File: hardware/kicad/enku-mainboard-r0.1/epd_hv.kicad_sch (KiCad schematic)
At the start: 2 parts

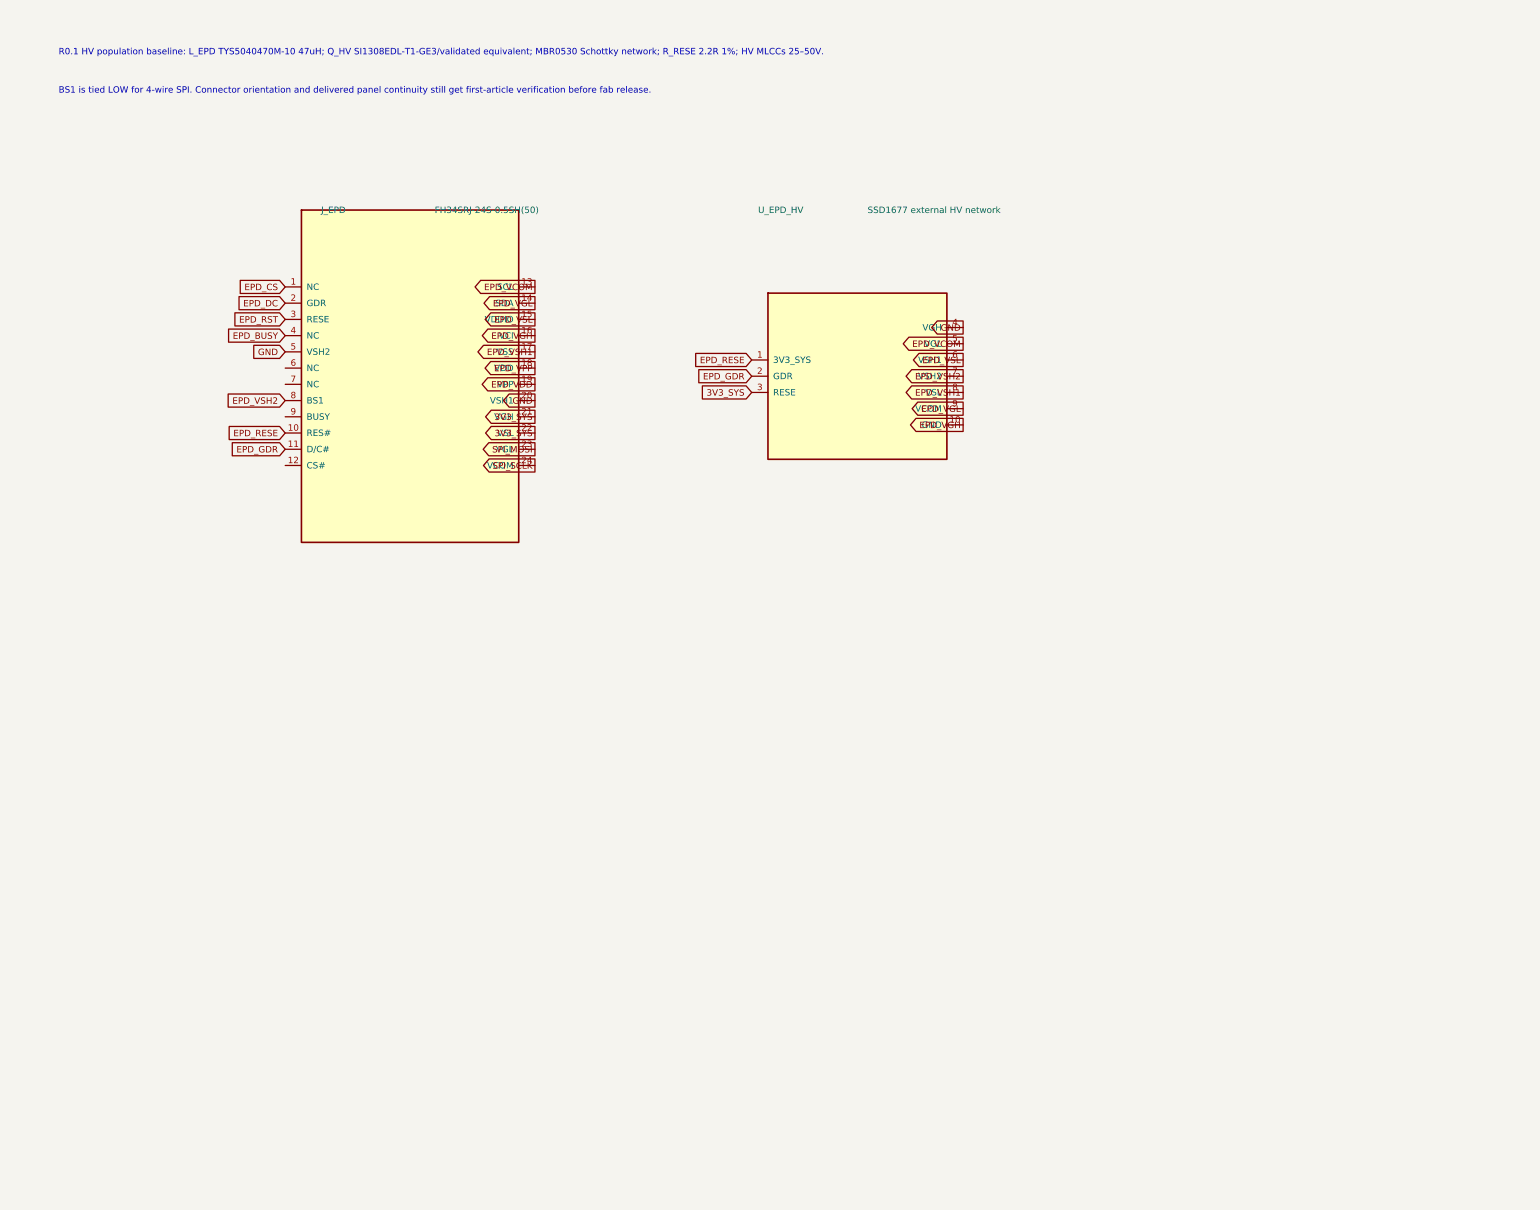
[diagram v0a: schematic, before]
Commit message: Expand SSD1677 EPD HV reference circuit to discretes
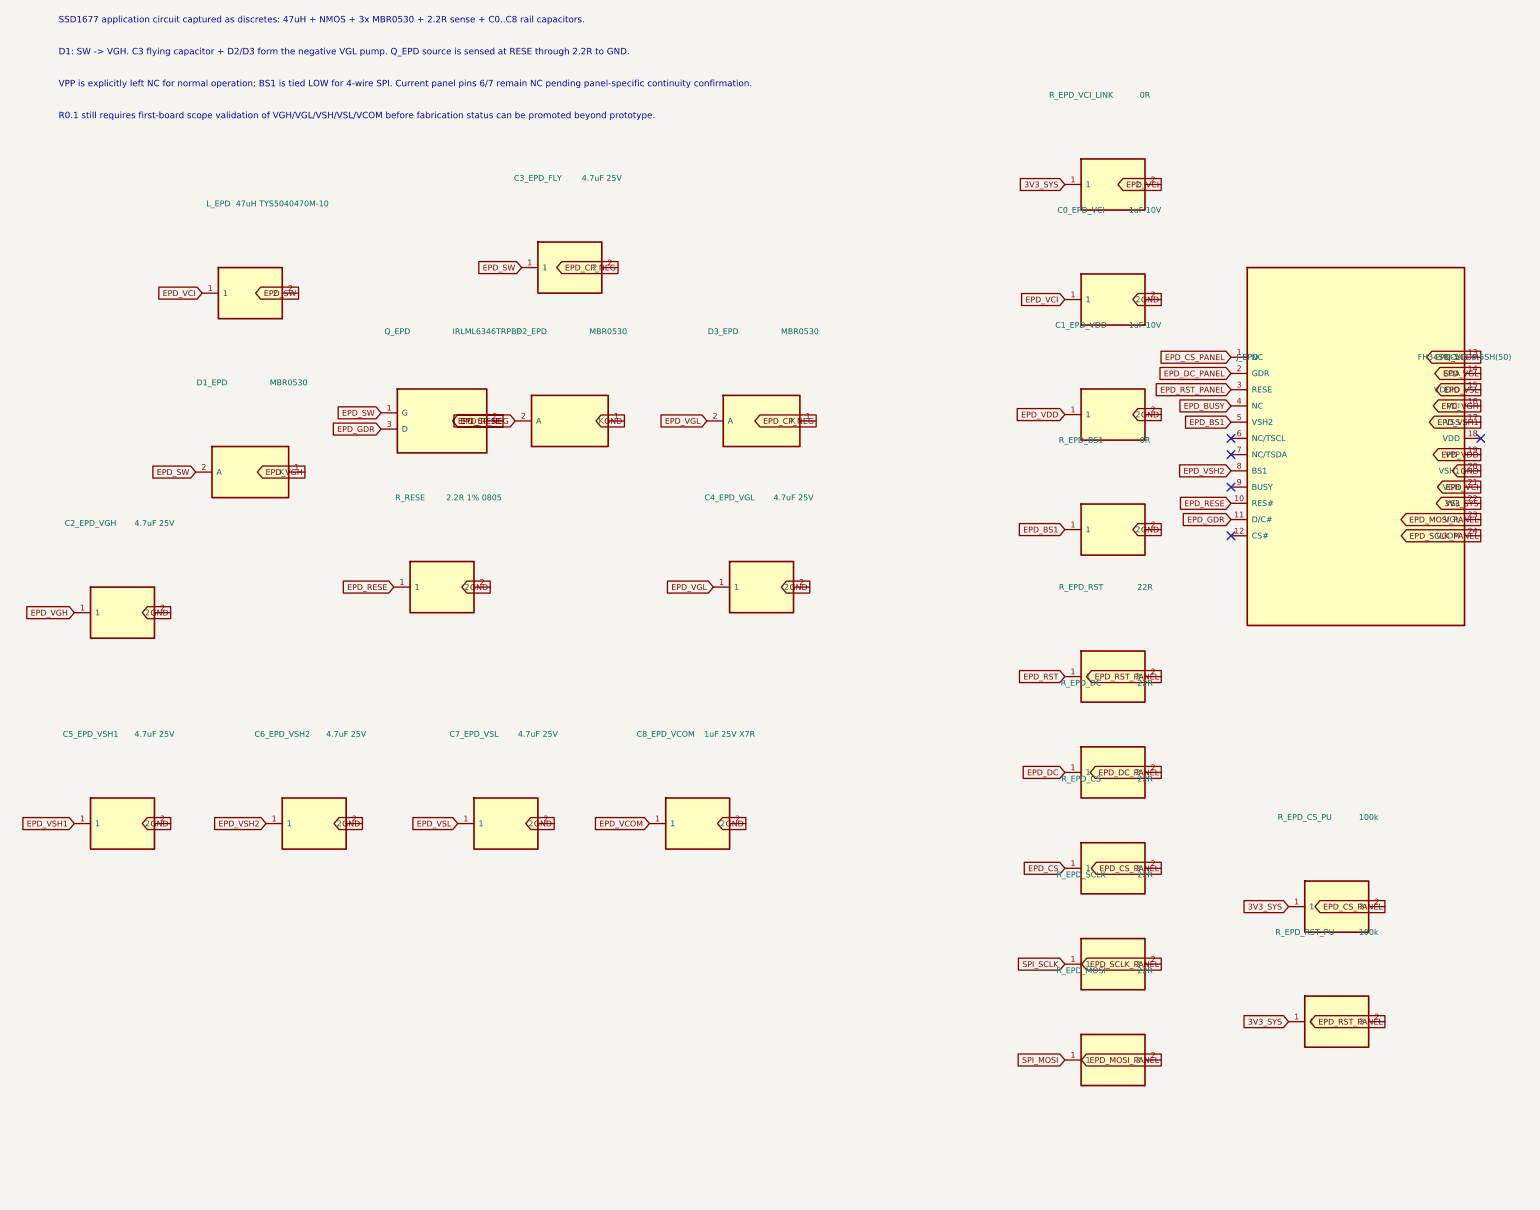
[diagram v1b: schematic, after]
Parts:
- removed J_EPD: FH34SRJ-24S-0.5SH(50), ENKU:R0.1_FH34SRJ_24_DUAL_CONTACT_PLACEHOLDER, symbol ENKU:EPD_FPC_24
- removed U_EPD_HV: SSD1677 external HV network, symbol ENKU:EPD_HV_NETWORK
- added C0_EPD_VCI, C1_EPD_VDD: 1uF 10V, Capacitor_SMD:C_0603_1608Metric, symbol ENKU:C
- added C2_EPD_VGH, C3_EPD_FLY, C4_EPD_VGL, C5_EPD_VSH1, C6_EPD_VSH2, C7_EPD_VSL: 4.7uF 25V, Capacitor_SMD:C_0805_2012Metric, symbol ENKU:C
- added C8_EPD_VCOM: 1uF 25V X7R, Capacitor_SMD:C_0805_2012Metric, symbol ENKU:C
- added D1_EPD, D2_EPD, D3_EPD: MBR0530, Diode_SMD:D_SOD-123, symbol ENKU:D_SCHOTTKY
- added J_EPD: FH34SRJ-24S-0.5SH(50), ENKU:R0.1_FH34SRJ_24_DUAL_CONTACT_PLACEHOLDER, symbol ENKU:EPD_FPC24
- added L_EPD: 47uH TYS5040470M-10, ENKU:TYS5040470M-10, symbol ENKU:L
- added Q_EPD: IRLML6346TRPBF, Package_TO_SOT_SMD:SOT-23, symbol ENKU:NMOS
- added R_EPD_BS1, R_EPD_VCI_LINK: 0R, Resistor_SMD:R_0603_1608Metric, symbol ENKU:R
- added R_EPD_CS, R_EPD_DC, R_EPD_MOSI, R_EPD_RST, R_EPD_SCLK: 22R, Resistor_SMD:R_0603_1608Metric, symbol ENKU:R
- added R_EPD_CS_PU, R_EPD_RST_PU: 100k, Resistor_SMD:R_0603_1608Metric, symbol ENKU:R
- added R_RESE: 2.2R 1% 0805, Resistor_SMD:R_0805_2012Metric, symbol ENKU:R
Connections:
- net 3V3_SYS: now also J_EPD.22 (VSL), R_EPD_CS_PU.1, R_EPD_RST_PU.1, R_EPD_VCI_LINK.1
- net EPD_BUSY: now also J_EPD.4 (NC)
- net EPD_CS: now also R_EPD_CS.1
- net EPD_DC: now also R_EPD_DC.1
- net EPD_GDR: now also J_EPD.11 (D/C#), Q_EPD.3 (D)
- net EPD_RESE: now also J_EPD.10 (RES#), Q_EPD.2 (S), R_RESE.1
- net EPD_RST: now also R_EPD_RST.1
- net EPD_VCOM: now also C8_EPD_VCOM.1, J_EPD.13 (SCL)
- net EPD_VDD: now also C1_EPD_VDD.1, J_EPD.19 (VPP)
- net EPD_VGH: now also C2_EPD_VGH.1, D1_EPD.1 (K), J_EPD.16 (VCI)
- net EPD_VGL: now also C4_EPD_VGL.1, D3_EPD.2 (A), J_EPD.14 (SDA)
- net EPD_VSH1: now also C5_EPD_VSH1.1, J_EPD.17 (VSS)
- net EPD_VSH2: now also C6_EPD_VSH2.1, J_EPD.8 (BS1)
- net EPD_VSL: now also C7_EPD_VSL.1, J_EPD.15 (VDDIO)
- net GND: now also C0_EPD_VCI.2, C1_EPD_VDD.2, C2_EPD_VGH.2, C4_EPD_VGL.2, C5_EPD_VSH1.2, C6_EPD_VSH2.2, C7_EPD_VSL.2, C8_EPD_VCOM.2, D2_EPD.1 (K), J_EPD.20 (VSH1), R_EPD_BS1.2, R_RESE.2
- net SPI_MOSI: now also R_EPD_MOSI.1
- net SPI_SCLK: now also R_EPD_SCLK.1
- new net EPD_BS1: J_EPD.5 (VSH2), R_EPD_BS1.1
- new net EPD_CP_NEG: C3_EPD_FLY.2, D2_EPD.2 (A), D3_EPD.1 (K)
- new net EPD_CS_PANEL: J_EPD.1 (NC), R_EPD_CS.2, R_EPD_CS_PU.2
- new net EPD_DC_PANEL: J_EPD.2 (GDR), R_EPD_DC.2
- new net EPD_MOSI_PANEL: J_EPD.23 (VGL), R_EPD_MOSI.2
- new net EPD_RST_PANEL: J_EPD.3 (RESE), R_EPD_RST.2, R_EPD_RST_PU.2
- new net EPD_SCLK_PANEL: J_EPD.24 (VCOM), R_EPD_SCLK.2
- new net EPD_SW: C3_EPD_FLY.1, D1_EPD.2 (A), L_EPD.2, Q_EPD.1 (G)
- new net EPD_VCI: C0_EPD_VCI.1, J_EPD.21 (VGH), L_EPD.1, R_EPD_VCI_LINK.2
- no-connect marks 0 -> 5
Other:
- note added: "D1: SW -> VGH. C3 flying capacitor + D2/D3 form the negative VGL pump. Q_EPD source is sensed at RESE through 2.2R to GND."
- note added: "R0.1 still requires first-board scope validation of VGH/VGL/VSH/VSL/VCOM before fabrication status can be promoted beyond prototype."
- note added: "SSD1677 application circuit captured as discretes: 47uH + NMOS + 3x MBR0530 + 2.2R sense + C0..C8 rail capacitors."
- note added: "VPP is explicitly left NC for normal operation; BS1 is tied LOW for 4-wire SPI. Current panel pins 6/7 remain NC pending panel-specific continuity confirmation."
- note removed: "BS1 is tied LOW for 4-wire SPI. Connector orientation and delivered panel continuity still get first-article verification before fab release."
- note removed: "R0.1 HV population baseline: L_EPD TYS5040470M-10 47uH; Q_HV SI1308EDL-T1-GE3/validated equivalent; MBR0530 Schottky network; R_RESE 2.2R 1%; HV MLCCs 25–50V."
- title: ENKU R0.1 — EPD + HV -> ENKU R0.1 — SSD1677 EPD + HV

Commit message: Align EPD boost baseline with current 3.97-inch application circuit
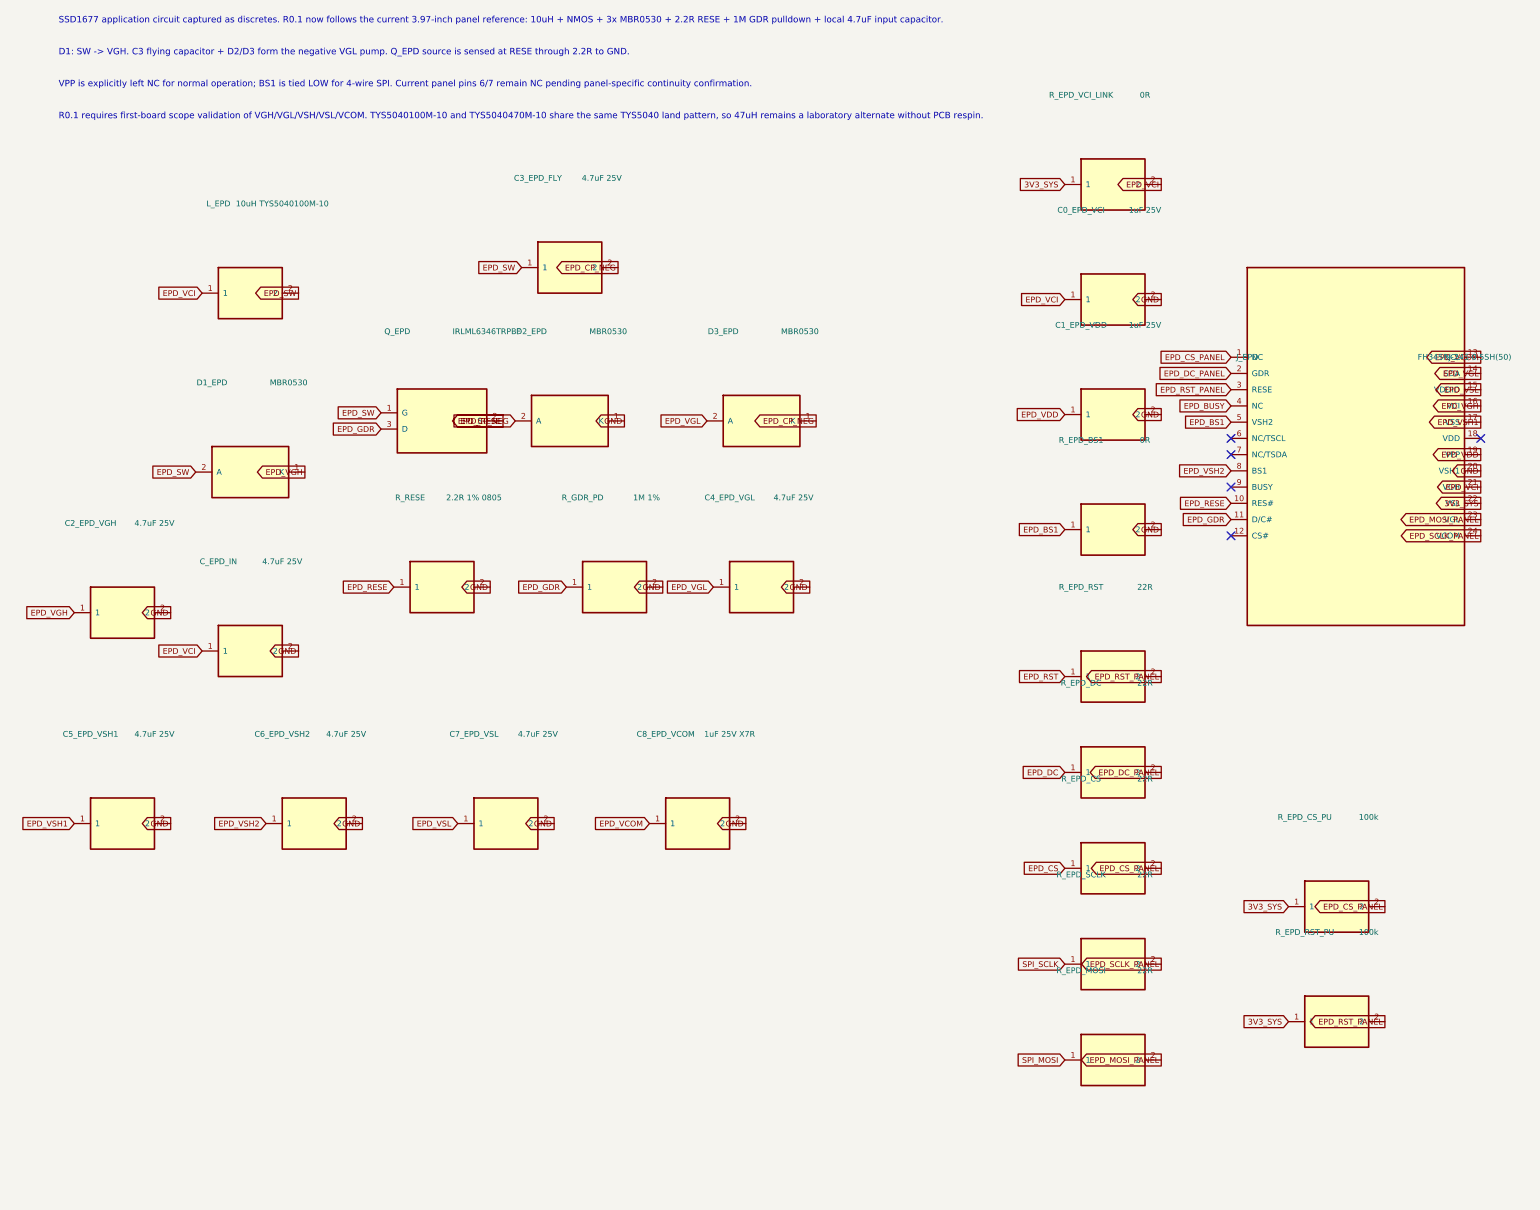
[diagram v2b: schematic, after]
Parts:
- added C_EPD_IN: 4.7uF 25V, Capacitor_SMD:C_0805_2012Metric, symbol ENKU:C
- added R_GDR_PD: 1M 1%, Resistor_SMD:R_0603_1608Metric, symbol ENKU:R
- C0_EPD_VCI, C1_EPD_VDD: value 1uF 10V -> 1uF 25V
- L_EPD: value 47uH TYS5040470M-10 -> 10uH TYS5040100M-10; footprint ENKU:TYS5040470M-10 -> ENKU:TYS5040_5x5
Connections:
- net EPD_GDR: now also R_GDR_PD.1
- net EPD_VCI: now also C_EPD_IN.1
- net GND: now also C_EPD_IN.2, R_GDR_PD.2
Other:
- note added: "R0.1 requires first-board scope validation of VGH/VGL/VSH/VSL/VCOM. TYS5040100M-10 and TYS5040470M-10 share the same TYS5040 land pattern, so 47uH remains a laboratory alternate without PCB respin."
- note added: "SSD1677 application circuit captured as discretes. R0.1 now follows the current 3.97-inch panel reference: 10uH + NMOS + 3x MBR0530 + 2.2R RESE + 1M GDR pulldown + local 4.7uF input capacitor."
- note removed: "R0.1 still requires first-board scope validation of VGH/VGL/VSH/VSL/VCOM before fabrication status can be promoted beyond prototype."
- note removed: "SSD1677 application circuit captured as discretes: 47uH + NMOS + 3x MBR0530 + 2.2R sense + C0..C8 rail capacitors."
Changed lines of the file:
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@@
 	(symbol (lib_id "ENKU:C") (at 190 63 0) (unit 1) (exclude_from_sim no) (in_bom yes) (on_board yes) (dnp no)
 		(property "Reference" "C0_EPD_VCI" (at 185 49 0) (effects (font (size 0.9 0.9))))
-		(property "Value" "1uF 10V" (at 195 49 0) (effects (font (size 0.9 0.9))))
+		(property "Value" "1uF 25V" (at 195 49 0) (effects (font (size 0.9 0.9))))
 		(property "Footprint" "Capacitor_SMD:C_0603_1608Metric" (at 190 63 0) (effects (font (size 0.9 0.9)) (hide yes)))
 		(property "Datasheet" "~" (at 190 63 0) (effects (font (size 0.9 0.9)) (hide yes)))
-		(property "Description" "1uF 10V" (at 190 63 0) (effects (font (size 0.9 0.9)) (hide yes)))
+		(property "Description" "1uF 25V" (at 190 63 0) (effects (font (size 0.9 0.9)) (hide yes)))
 		(pin "1")
 		(pin "2")
@@
 	(symbol (lib_id "ENKU:C") (at 190 81 0) (unit 1) (exclude_from_sim no) (in_bom yes) (on_board yes) (dnp no)
 		(property "Reference" "C1_EPD_VDD" (at 185 67 0) (effects (font (size 0.9 0.9))))
-		(property "Value" "1uF 10V" (at 195 67 0) (effects (font (size 0.9 0.9))))
+		(property "Value" "1uF 25V" (at 195 67 0) (effects (font (size 0.9 0.9))))
 		(property "Footprint" "Capacitor_SMD:C_0603_1608Metric" (at 190 81 0) (effects (font (size 0.9 0.9)) (hide yes)))
 		(property "Datasheet" "~" (at 190 81 0) (effects (font (size 0.9 0.9)) (hide yes)))
-		(property "Description" "1uF 10V" (at 190 81 0) (effects (font (size 0.9 0.9)) (hide yes)))
+		(property "Description" "1uF 25V" (at 190 81 0) (effects (font (size 0.9 0.9)) (hide yes)))
 		(pin "1")
 		(pin "2")
@@
 	(symbol (lib_id "ENKU:L") (at 55 62 0) (unit 1) (exclude_from_sim no) (in_bom yes) (on_board yes) (dnp no)
 		(property "Reference" "L_EPD" (at 50 48 0) (effects (font (size 0.9 0.9))))
-		(property "Value" "47uH TYS5040470M-10" (at 60 48 0) (effects (font (size 0.9 0.9))))
-		(property "Footprint" "ENKU:TYS5040470M-10" (at 55 62 0) (effects (font (size 0.9 0.9)) (hide yes)))
+		(property "Value" "10uH TYS5040100M-10" (at 60 48 0) (effects (font (size 0.9 0.9))))
+		(property "Footprint" "ENKU:TYS5040_5x5" (at 55 62 0) (effects (font (size 0.9 0.9)) (hide yes)))
 		(property "Datasheet" "~" (at 55 62 0) (effects (font (size 0.9 0.9)) (hide yes)))
-		(property "Description" "47uH TYS5040470M-10" (at 55 62 0) (effects (font (size 0.9 0.9)) (hide yes)))
+		(property "Description" "10uH TYS5040100M-10" (at 55 62 0) (effects (font (size 0.9 0.9)) (hide yes)))
 		(pin "1")
 		(pin "2")
@@
 	(global_label "EPD_VCOM" (shape input) (at 117.46 145 0) (effects (font (size 0.9 0.9)) (justify right bottom)))
 	(global_label "GND" (shape output) (at 132.54 145 180) (effects (font (size 0.9 0.9)) (justify right bottom)))
-	(text "SSD1677 application circuit captured as discretes: 47uH + NMOS + 3x MBR0530 + 2.2R sense + C0..C8 rail capacitors." (exclude_from_sim no) (at 25 20 0) (effects (font (size 1.0 1.0)) (justify left bottom)))
+	(symbol (lib_id "ENKU:R") (at 112 108 0) (unit 1) (exclude_from_sim no) (in_bom yes) (on_board yes) (dnp no)
+		(property "Reference" "R_GDR_PD" (at 107 94 0) (effects (font (size 0.9 0.9))))
+		(property "Value" "1M 1%" (at 117 94 0) (effects (font (size 0.9 0.9))))
+		(property "Footprint" "Resistor_SMD:R_0603_1608Metric" (at 112 108 0) (effects (font (size 0.9 0.9)) (hide yes)))
+		(property "Datasheet" "~" (at 112 108 0) (effects (font (size 0.9 0.9)) (hide yes)))
+		(property "Description" "GDR gate pulldown from current 3.97-inch SSD1677 application circuit" (at 112 108 0) (effects (font (size 0.9 0.9)) (hide yes)))
+		(pin "1")
+		(pin "2")
+		(instances (project "enku-mainboard-r0.1" (path "/10000000-0000-4000-8000-000000000001/10000000-0000-4000-8000-000000000030" (reference "R_GDR_PD") (unit 1))))
+	)
+	(global_label "EPD_GDR" (shape input) (at 104.46 108 0) (effects (font (size 0.9 0.9)) (justify right bottom)))
+	(global_label "GND" (shape output) (at 119.54 108 180) (effects (font (size 0.9 0.9)) (justify right bottom)))
+	(symbol (lib_id "ENKU:C") (at 55 118 0) (unit 1) (exclude_from_sim no) (in_bom yes) (on_board yes) (dnp no)
+		(property "Reference" "C_EPD_IN" (at 50 104 0) (effects (font (size 0.9 0.9))))
+		(property "Value" "4.7uF 25V" (at 60 104 0) (effects (font (size 0.9 0.9))))
+		(property "Footprint" "Capacitor_SMD:C_0805_2012Metric" (at 55 118 0) (effects (font (size 0.9 0.9)) (hide yes)))
+		(property "Datasheet" "~" (at 55 118 0) (effects (font (size 0.9 0.9)) (hide yes)))
+		(property "Description" "Local SSD1677 booster input capacitor, current 3.97-inch application circuit" (at 55 118 0) (effects (font (size 0.9 0.9)) (hide yes)))
+		(pin "1")
+		(pin "2")
+		(instances (project "enku-mainboard-r0.1" (path "/10000000-0000-4000-8000-000000000001/10000000-0000-4000-8000-000000000030" (reference "C_EPD_IN") (unit 1))))
+	)
+	(global_label "EPD_VCI" (shape input) (at 47.46 118 0) (effects (font (size 0.9 0.9)) (justify right bottom)))
+	(global_label "GND" (shape output) (at 62.54 118 180) (effects (font (size 0.9 0.9)) (justify right bottom)))
+	(text "SSD1677 application circuit captured as discretes. R0.1 now follows the current 3.97-inch panel reference: 10uH + NMOS + 3x MBR0530 + 2.2R RESE + 1M GDR pulldown + local 4.7uF input capacitor." (exclude_from_sim no) (at 25 20 0) (effects (font (size 1.0 1.0)) (justify left bottom)))
 	(text "D1: SW -> VGH. C3 flying capacitor + D2/D3 form the negative VGL pump. Q_EPD source is sensed at RESE through 2.2R to GND." (exclude_from_sim no) (at 25 25 0) (effects (font (size 1.0 1.0)) (justify left bottom)))
 	(text "VPP is explicitly left NC for normal operation; BS1 is tied LOW for 4-wire SPI. Current panel pins 6/7 remain NC pending panel-specific continuity confirmation." (exclude_from_sim no) (at 25 30 0) (effects (font (size 1.0 1.0)) (justify left bottom)))
-	(text "R0.1 still requires first-board scope validation of VGH/VGL/VSH/VSL/VCOM before fabrication status can be promoted beyond prototype." (exclude_from_sim no) (at 25 35 0) (effects (font (size 1.0 1.0)) (justify left bottom)))
+	(text "R0.1 requires first-board scope validation of VGH/VGL/VSH/VSL/VCOM. TYS5040100M-10 and TYS5040470M-10 share the same TYS5040 land pattern, so 47uH remains a laboratory alternate without PCB respin." (exclude_from_sim no) (at 25 35 0) (effects (font (size 1.0 1.0)) (justify left bottom)))
 	(sheet_instances (path "/" (page "4")))
 )
